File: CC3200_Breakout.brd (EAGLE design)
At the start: 58.4 x 35.2 mm, 51 parts, among them J22 M10X2, J23 M10X2, U15 AT25FS010, Y2 32.768KHz, Y3 407MHz

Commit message: proper files added now, ready to finish routing
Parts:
- added C1, C11, C13, C14, C16, C17, C19, C21, C22, C5, C51, C9: 0.1uF, SparkFun-Capacitors:0402
- added C10, C12, C2, C20, C6: 1.0uF, SparkFun-Capacitors:0402
- added C15, C18: 4.7nF, SparkFun-Retired:0603
- added C3, C4, C7: 10uF, SparkFun-Capacitors:0603
- added C46, C49: 47uF, SparkFun-Capacitors:0603
- added C52: 100uF, SparkFun-Capacitors:PANASONIC_D
- added C53: 0.1uF, resistor:C0402K
- added D1: 1A/30V, diode:SMB
- added FB1, FB2: 40Ω/1.5A, SparkFun-Coils:0603
- added J1: MJ-3536N, con-cuistack:MJ-3536N
- added J2: (no value), SparkFun-Connectors:USB-MICROB
- added J3, J4: SJ-3515-SMT, con-cuistack:SJ-3515-SMT
- added JMP1, JMP2, JMP3, JMP4, JMP5: 0R-JUMPA, jump-0r-smd:A0R-JMP
- added JP1: (no value), SparkFun-Retired:1X02
- added R2, R5, R7: 10k, SparkFun-Resistors:0603
- added R3, R4: 1k, SparkFun-Resistors:0603
- added TERMINAL_BLOCK: (no value), SparkFun-Connectors:JST-4-PTH
- added TP1, TP13, TP2, TP3: (no value), SparkFun-Connectors:1X01
- added U1: TLV320AIC3254_RHB_32, TLV320AIC3254:RHB32_3P45X3P45
- added U2: TPA2012D2_RTJ_20, TPA2012D2_RTJ_20:RTJ20_2P7X2P7
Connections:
- removed net 50: J22.20, U$1.50
- removed net 53: J22.16, U$1.53
- removed net 61: J22.9, U$1.61
- removed net 63: J22.14, U$1.63
- removed net 64: J22.18, U$1.64
- removed net N$91: J23.10
- new net +3V3: C5.1, C6.1, U1.26
- new net AA_LOL: R4.2, U1.22
- new net AA_LOR: R3.2, U1.23
- new net BCLK_IN: JMP3.2, TP13.1, U1.1, U1.2
- new net BCLK_J3: J22.16, JMP3.1, U$1.53
- new net CODEC_RESET: J22.9, JMP1.3, U$1.61
- new net DIN: JMP4.1, JMP5.3, U1.4
- new net DIN_J3: J22.18, JMP4.2, U$1.64
- new net DOUT: JMP4.3, JMP5.1, U1.5
- new net DOUT_J3: J22.20, JMP5.2, U$1.50
- new net FSYNC_IN: JMP2.2, U1.3
- new net FSYNC_J3: J22.14, JMP2.1, U$1.63
- new net LOUT1: TERMINAL_BLOCK.4, U2.2
- new net LOUT2: TERMINAL_BLOCK.3, U2.5
- new net MASTER_RESET: C53.1, J23.10, JMP1.1, R7.1
- new net MICBIAS: R5.2, U1.19
- new net N$23: TP2.1, U1.11
- new net N$25: C3.1, U1.18
- new net N$26: TP1.1, U1.8
- new net N$34: TP3.1, U1.32
- new net N$35: JP1.2, R2.2, U2.1
- new net N$37: C7.1, U1.29
- new net N$38: C22.2, J4.3, J4.4
- new net N$39: C14.2, U2.20
- new net N$41: C13.1, C15.1, R3.1
- new net N$42: C13.2, U2.19
- new net N$43: C16.2, U2.17
- new net N$44: C16.1, C18.1, R4.1
- new net N$45: C17.2, U2.16
- new net N$46: C21.2, J4.1, J4.2
- new net N$55: C46.2, J3.1, J3.2
- new net N$56: C49.2, J3.3, J3.4
- new net N$57: C51.2, J1.2, J1.3, R5.1
- new net N$58: D1.A, FB2.2
- new net N$59: FB2.1, J2.VBUS
- new net N$60: FB1.2, J2.GND
- new net RESET_OUT: JMP1.2, U1.31
- new net ROUT1: TERMINAL_BLOCK.2, U2.14
- new net ROUT2: TERMINAL_BLOCK.1, U2.11
- new net SJ_HPL: C49.1, U1.25
- new net SJ_HPR: C46.1, U1.27
- new net SJ_IN1L: C21.1, U1.13
- new net SJ_IN1R: C22.1, U1.14
- new net SJ_IN2L: U1.15
- new net SJ_IN2R: C51.1, U1.16
- new net SJ_IN3L: U1.20
- new net SJ_IN3R: U1.21
- new net VCCA: C4.1, U1.24, U2.7, U2.8
- new net VCC_5V_MCU: D1.C
- new net VCC_BRD1: C1.1, C10.1, C11.1, C12.1, C19.1, C2.1, C20.1, C52.+, C9.1, JP1.1, U1.30, U1.6, U2.13, U2.3, U2.9
- net 3.3V: now also R7.2
- net GND: now also C1.2, C10.2, C11.2, C12.2, C14.1, C15.2, C17.1, C18.2, C19.2, C2.2, C20.2, C3.2, C4.2, C5.2, C52.-, C53.2, C6.2, C7.2, C9.2, FB1.1, J1.1, J2.MT1, J2.MT2, J2.P$1, J2.P$2, J3.5, J4.5, R2.1, U1.12, U1.17, U1.28, U1.33, U1.7, U2.12, U2.15, U2.18, U2.21, U2.4
- net SCL: now also U1.9
- net SDA: now also U1.10
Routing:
- net DOUT_J3: track 0.00 -> 60.7 mm, vias 0 -> 1
- net 50: track 60.7 -> 0.00 mm, vias 1 -> 0
- net BCLK_J3: track 0.00 -> 45.4 mm, vias 0 -> 3
- net 53: track 45.4 -> 0.00 mm, vias 3 -> 0
- net DIN_J3: track 0.00 -> 27.4 mm, vias 0 -> 1
- net 64: track 27.4 -> 0.00 mm, vias 1 -> 0
- net FSYNC_J3: track 0.00 -> 24.1 mm, vias 0 -> 1
- net 63: track 24.1 -> 0.00 mm, vias 1 -> 0
- net CODEC_RESET: track 0.00 -> 24.1 mm, vias 0 -> 1
- net 61: track 24.1 -> 0.00 mm, vias 1 -> 0
- removed copper zone on layer 1, net GND
- removed copper zone on layer 2, net GND
- removed copper zone on layer 16, net VCC_BRD
- removed copper zone on layer 15, net V_BATT
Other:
- board size 58.4 x 35.2 mm -> 76.2 x 50.8 mm

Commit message: routed
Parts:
- moved JMP1 399.8 mm to (13.5, 69.6), turned to 270 degrees
- moved R7 387.3 mm to (35.0, 37.2), turned to 270 degrees
- moved C53 383.2 mm to (31.6, 37.6), turned to 270 degrees
- moved JMP4 367.9 mm to (19.2, 50.8)
- moved JMP5 366.8 mm to (18.9, 40.7)
- moved JMP2 362.1 mm to (21.3, 61.3)
- moved JMP3 349.7 mm to (14.2, 42.0), turned to 180 degrees
- moved D1 324.9 mm to (59.1, 22.5), turned to 270 degrees
- moved FB2 316.8 mm to (61.5, 14.2), turned to 90 degrees
- moved J2 314.1 mm to (59.7, 3.81), turned to 90 degrees
- moved FB1 312.0 mm to (58.5, 13.7), turned to 270 degrees
- moved C49 288.9 mm to (10.6, 73.6), turned to 180 degrees
- moved C46 287.5 mm to (18.0, 73.5), turned to 90 degrees
- moved C21 285.1 mm to (31.2, 73.5), turned to 90 degrees
- moved C52 272.4 mm to (4.39, 69.4), turned to 180 degrees
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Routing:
- net GND: track 9.93 -> 766.8 mm, vias 49 -> 67
- net VCC_BRD1: track 0.00 -> 121.2 mm, vias 0 -> 5
- net MASTER_RESET: track 0.00 -> 86.5 mm, vias 0 -> 2
- net SCL: track 30.5 -> 107.8 mm, vias 1 -> 2
- net N$35: track 0.00 -> 74.0 mm, vias 0 -> 2
- net FSYNC_J3: track 24.1 -> 88.3 mm, vias 1 -> 3
- net SDA: track 32.2 -> 95.2 mm, vias 1 -> 2
- net DIN_J3: track 27.4 -> 90.2 mm, vias 1 -> 3
- net V_BATT: track 94.1 -> 153.0 mm, vias 8 -> 13
- net N$45: track 0.00 -> 55.2 mm, vias 0 -> 2
- net CODEC_RESET: track 24.1 -> 75.2 mm, vias 1 -> 4
- net BCLK_IN: track 0.00 -> 45.6 mm, vias 0 -> 1
- net SJ_IN1L: track 0.00 -> 39.0 mm, vias 0 -> 2
- net SJ_HPL: track 0.00 -> 32.2 mm, vias 0 -> 2
- net SJ_IN1R: track 0.00 -> 30.5 mm
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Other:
- board size 76.2 x 50.8 mm -> 76.2 x 88.9 mm

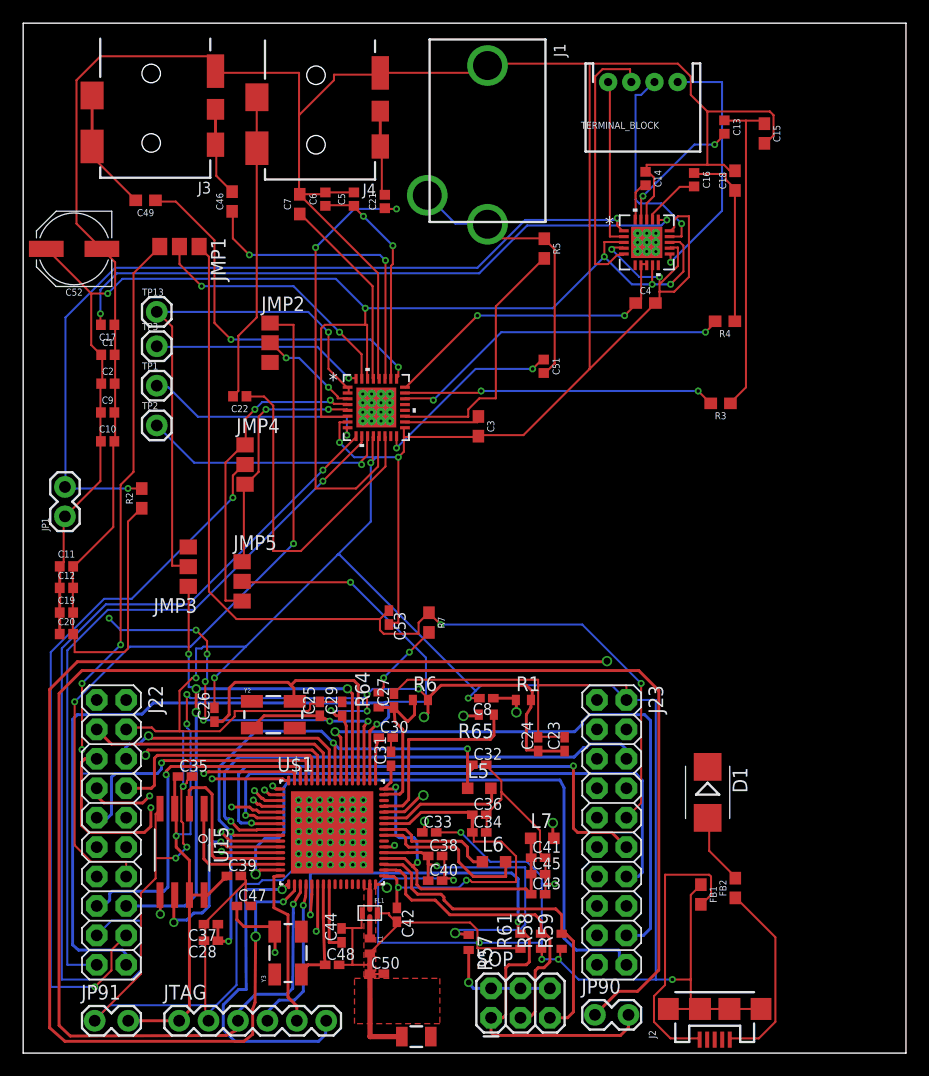
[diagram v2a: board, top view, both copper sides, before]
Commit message: routing finished, BOM added
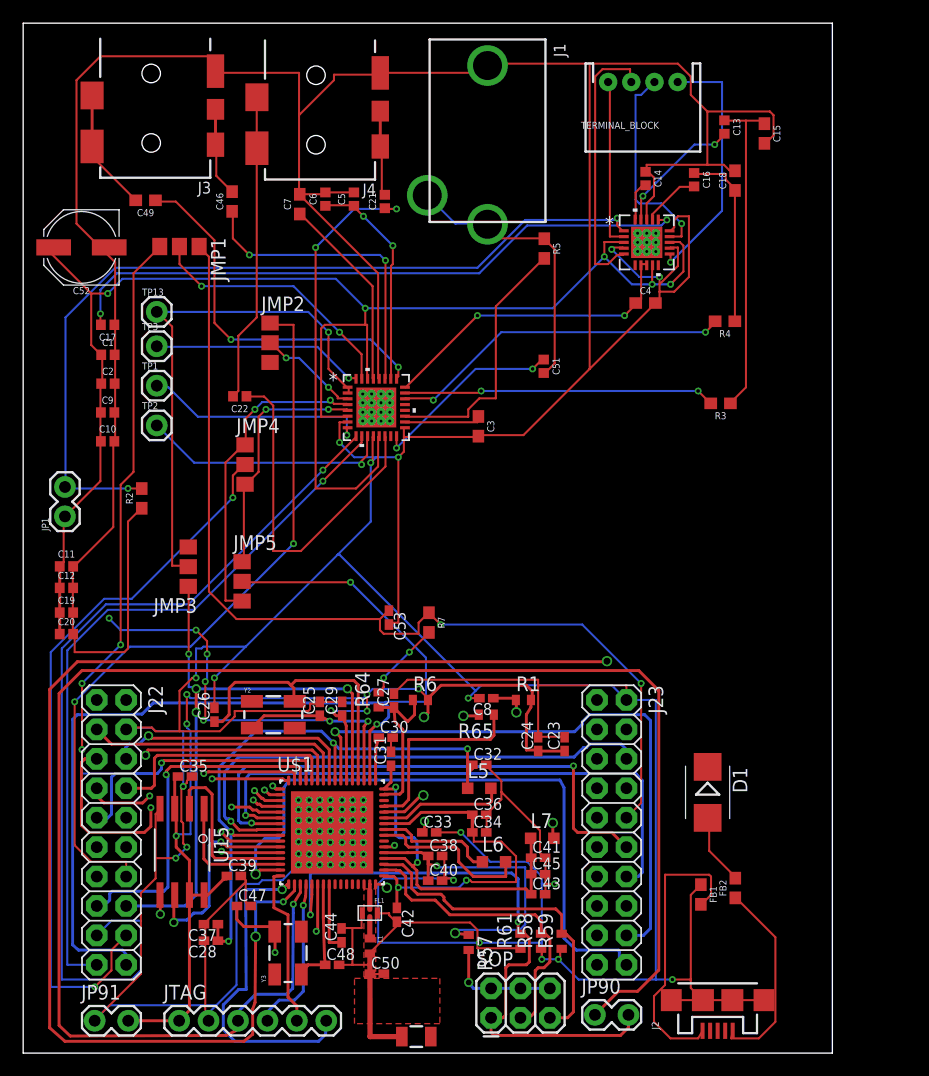
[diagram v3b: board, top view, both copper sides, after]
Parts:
- moved J2 0.80 mm to (59.9, 4.57)
- moved C52 0.65 mm to (5.03, 69.5)
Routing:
- net N$60: track 24.5 -> 25.1 mm
- net VCC_BRD1: track 121.2 -> 121.7 mm
- net GND: track 766.8 -> 767.3 mm
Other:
- board size 76.2 x 88.9 mm -> 69.8 x 88.9 mm
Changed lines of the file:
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@@
 <board>
 <plain>
-<wire x1="0" y1="0" x2="76.2" y2="0" width="0" layer="20"/>
-<wire x1="76.2" y1="0" x2="76.2" y2="88.9" width="0" layer="20"/>
-<wire x1="76.2" y1="88.9" x2="0" y2="88.9" width="0" layer="20"/>
+<wire x1="0" y1="0" x2="69.85" y2="0" width="0" layer="20"/>
+<wire x1="69.85" y1="0" x2="69.85" y2="88.9" width="0" layer="20"/>
+<wire x1="69.85" y1="88.9" x2="0" y2="88.9" width="0" layer="20"/>
 <wire x1="0" y1="88.9" x2="0" y2="0" width="0" layer="20"/>
 </plain>
@@
 <attribute name="PROD_ID" value="RES-00824" x="44.9834" y="69.4436" size="1.778" layer="27" rot="R270" display="off"/>
 </element>
-<element name="C52" library="SparkFun-Capacitors" package="PANASONIC_D" value="100uF" x="4.3942" y="69.4182" rot="R180">
-<attribute name="PROD_ID" value="CAP-12547" x="4.3942" y="69.4182" size="1.778" layer="27" rot="R180" display="off"/>
+<element name="C52" library="SparkFun-Capacitors" package="PANASONIC_D" value="100uF" x="5.0292" y="69.5452" rot="R180">
+<attribute name="PROD_ID" value="CAP-12547" x="5.0292" y="69.5452" size="1.778" layer="27" rot="R180" display="off"/>
 </element>
 <element name="TERMINAL_BLOCK" library="SparkFun-Connectors" package="JST-4-PTH" value="" x="53.4924" y="83.82" rot="R180">
@@
 </element>
 <element name="D1" library="diode" package="SMB" value="1A/30V" x="59.0804" y="22.5044" rot="R270"/>
-<element name="J2" library="SparkFun-Connectors" package="USB-MICROB" value="" x="59.69" y="3.81" rot="R90">
-<attribute name="PROD_ID" value="CONN-09505" x="59.69" y="3.81" size="1.778" layer="27" rot="R90" display="off"/>
-<attribute name="SF_ID" value="PRT-08533" x="59.69" y="3.81" size="1.778" layer="27" rot="R90" display="off"/>
+<element name="J2" library="SparkFun-Connectors" package="USB-MICROB" value="" x="59.944" y="4.572" rot="R90">
+<attribute name="PROD_ID" value="CONN-09505" x="59.944" y="4.572" size="1.778" layer="27" rot="R90" display="off"/>
+<attribute name="SF_ID" value="PRT-08533" x="59.944" y="4.572" size="1.778" layer="27" rot="R90" display="off"/>
 </element>
 <element name="JMP2" library="jump-0r-smd" package="A0R-JMP" value="0R-JUMPA" x="21.3106" y="61.3156"/>
@@
 <wire x1="7.9375" y1="68.2625" x2="6.82625" y2="69.37375" width="0.1778" layer="1"/>
 <wire x1="7.9375" y1="62.865" x2="7.9375" y2="68.2625" width="0.1778" layer="1"/>
-<wire x1="6.82625" y1="69.37375" x2="6.7942" y2="69.4182" width="0.1778" layer="1"/>
+<wire x1="6.82625" y1="69.37375" x2="7.4292" y2="69.5452" width="0.1778" layer="1"/>
 <wire x1="7.9375" y1="62.865" x2="7.8698" y2="62.865" width="0.1778" layer="1"/>
 <wire x1="7.77875" y1="45.4025" x2="4.445" y2="42.06875" width="0.1778" layer="1"/>
@@
 <wire x1="16.51" y1="86.0425" x2="6.6675" y2="86.0425" width="0.1778" layer="1"/>
 <wire x1="16.51" y1="84.7725" x2="16.51" y2="86.0425" width="0.1778" layer="1"/>
-<wire x1="6.6675" y1="69.5325" x2="6.7942" y2="69.4182" width="0.1778" layer="1"/>
+<wire x1="6.6675" y1="69.5325" x2="7.4292" y2="69.5452" width="0.1778" layer="1"/>
 <wire x1="16.51" y1="84.7725" x2="16.6006" y2="84.7594" width="0.1778" layer="1"/>
 <wire x1="26.82875" y1="84.455" x2="30.7975" y2="84.455" width="0.1778" layer="1"/>
@@
 <wire x1="30.7975" y1="84.455" x2="30.8246" y2="84.607" width="0.1778" layer="1"/>
 <wire x1="57.62625" y1="13.6525" x2="58.42" y2="14.44625" width="0.1778" layer="1"/>
-<wire x1="57.62625" y1="4.60375" x2="57.62625" y2="6.35" width="0.1778" layer="1"/>
-<wire x1="57.62625" y1="6.35" x2="57.62625" y2="13.6525" width="0.1778" layer="1"/>
+<wire x1="57.62625" y1="13.6525" x2="57.62625" y2="6.35" width="0.1778" layer="1"/>
 <wire x1="58.42" y1="14.44625" x2="58.4962" y2="14.5406" width="0.1778" layer="1"/>
-<wire x1="57.62625" y1="3.81" x2="55.69" y2="3.81" width="0.1778" layer="1"/>
-<wire x1="57.62625" y1="4.60375" x2="57.62625" y2="3.81" width="0.1778" layer="1"/>
-<wire x1="57.62625" y1="4.60375" x2="58.42" y2="3.81" width="0.1778" layer="1"/>
-<wire x1="58.42" y1="3.81" x2="60.96" y2="3.81" width="0.1778" layer="1"/>
-<wire x1="60.96" y1="3.81" x2="63.69" y2="3.81" width="0.1778" layer="1"/>
+<wire x1="58.674" y1="4.572" x2="61.214" y2="4.572" width="0.1778" layer="1"/>
+<wire x1="61.214" y1="4.572" x2="63.944" y2="4.572" width="0.1778" layer="1"/>
 <wire x1="29.21" y1="10.795" x2="28.41625" y2="10.795" width="0.1778" layer="1"/>
 <wire x1="28.41625" y1="10.795" x2="27.6225" y2="10.795" width="0.1778" layer="1"/>
@@
 <wire x1="31.75" y1="27.14625" x2="31.75" y2="26" width="0.1778" layer="1"/>
 <wire x1="31.75" y1="27.14625" x2="31.8928" y2="27.2288" width="0.1778" layer="1"/>
+<wire x1="55.944" y1="4.572" x2="58.674" y2="4.572" width="0.1778" layer="1"/>
+<wire x1="57.62625" y1="6.35" x2="57.62625" y2="5.61975" width="0.1778" layer="1"/>
+<wire x1="57.62625" y1="5.61975" x2="58.674" y2="4.572" width="0.1778" layer="1"/>
 <wire x1="53.8226" y1="71.952" x2="53.8226" y2="69.977" width="0" layer="19" extent="1-1"/>
 <wire x1="30.48" y1="55.7276" x2="30.7300625" y2="58.2026" width="0" layer="19" extent="1-1"/>
@@
 <wire x1="61.11875" y1="1.27" x2="63.5" y2="1.27" width="0.1778" layer="1"/>
 <wire x1="61.595" y1="13.335" x2="61.468" y2="13.3994" width="0.1778" layer="1"/>
-<wire x1="61.11875" y1="1.27" x2="60.99" y2="1.16" width="0.1778" layer="1"/>
+<wire x1="61.11875" y1="1.27" x2="61.244" y2="1.922" width="0.1778" layer="1"/>
 </signal>
 <signal name="N$60">
@@
 <wire x1="58.26125" y1="1.27" x2="55.88" y2="1.27" width="0.1778" layer="1"/>
 <wire x1="58.57875" y1="12.85875" x2="58.4962" y2="12.8406" width="0.1778" layer="1"/>
-<wire x1="58.26125" y1="1.27" x2="58.39" y2="1.16" width="0.1778" layer="1"/>
+<wire x1="58.26125" y1="1.27" x2="58.644" y2="1.922" width="0.1778" layer="1"/>
 </signal>
 <signal name="FSYNC_J3">
@@
 <wire x1="5.87375" y1="61.11875" x2="5.87375" y2="65.56375" width="0.1778" layer="1"/>
 <wire x1="6.6675" y1="60.325" x2="5.87375" y2="61.11875" width="0.1778" layer="1"/>
-<wire x1="2.06375" y1="69.37375" x2="1.9942" y2="69.4182" width="0.1778" layer="1"/>
+<wire x1="2.06375" y1="69.37375" x2="2.6292" y2="69.5452" width="0.1778" layer="1"/>
 <wire x1="6.6675" y1="60.325" x2="6.7352" y2="60.2742" width="0.1778" layer="1"/>
 <wire x1="6.6675" y1="49.37125" x2="3.65125" y2="46.355" width="0.1778" layer="1"/>

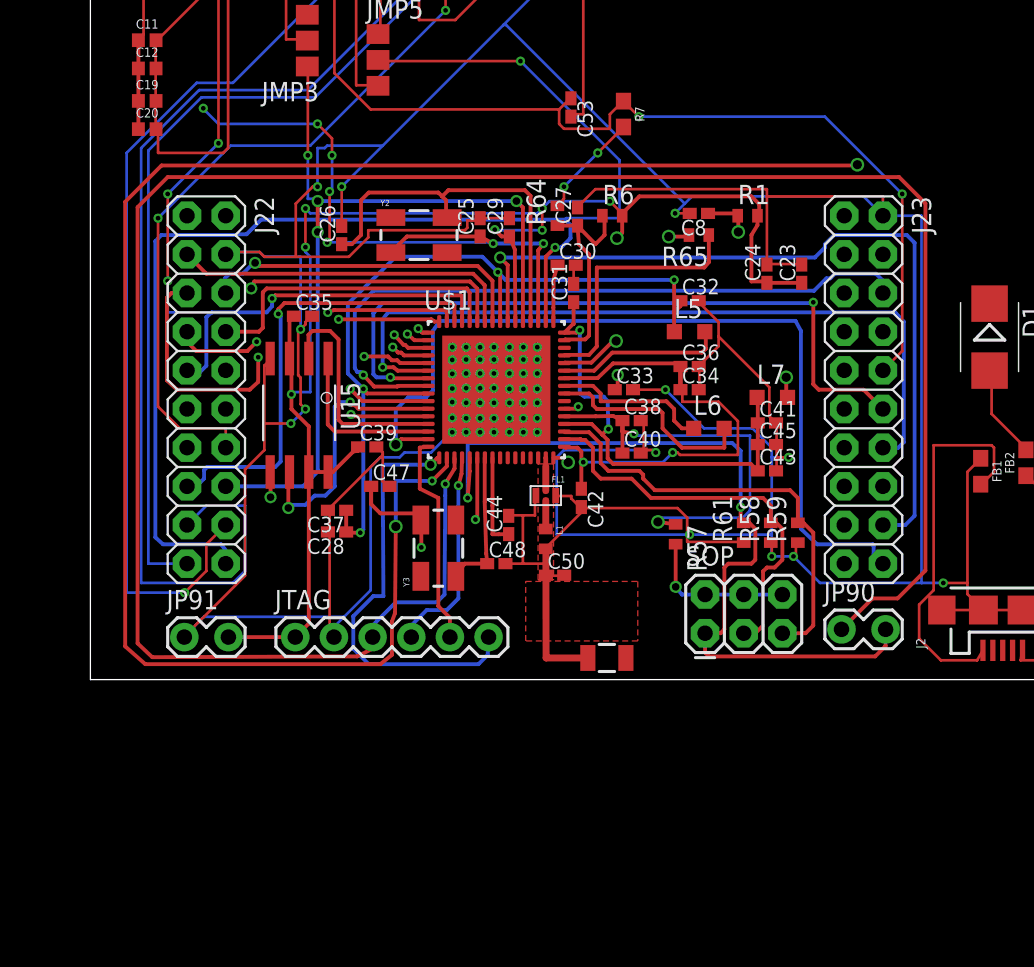
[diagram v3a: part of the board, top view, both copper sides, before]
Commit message: before ripup and change to two layers
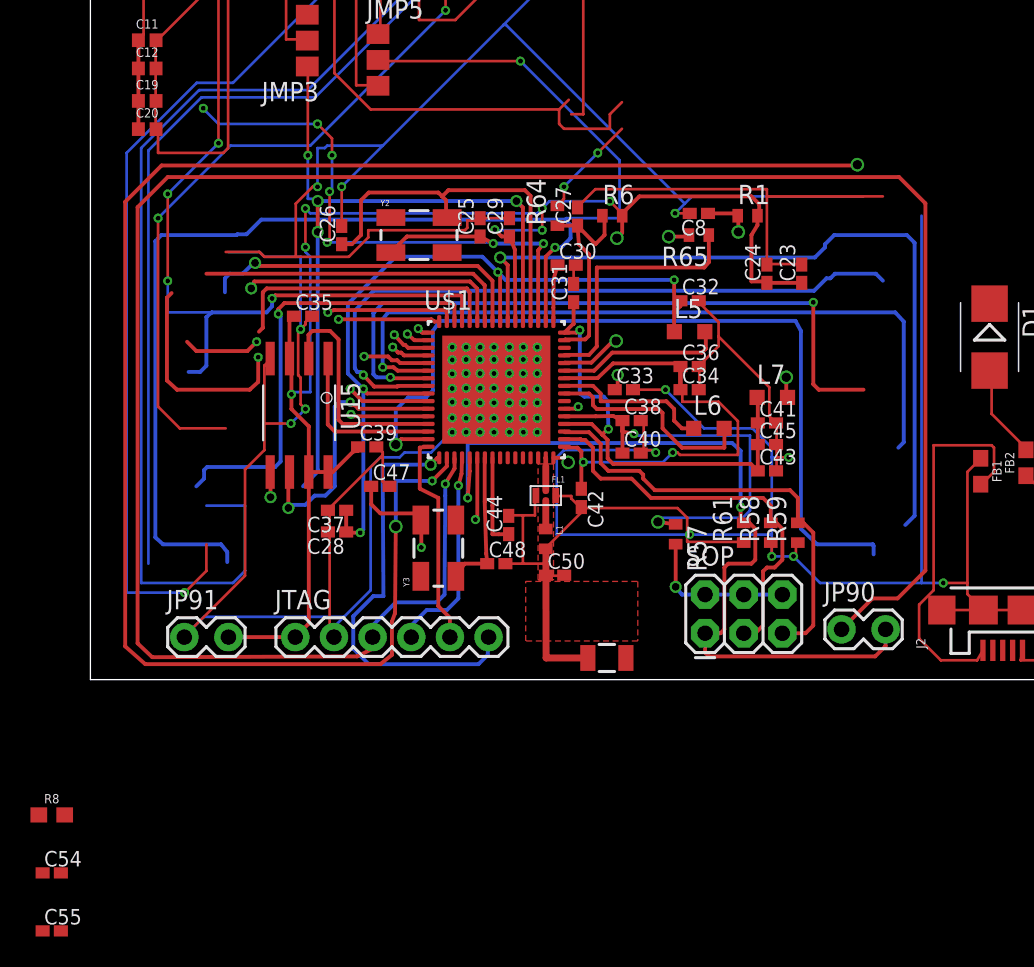
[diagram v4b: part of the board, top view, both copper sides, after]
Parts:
- removed C53: 0.1uF, resistor:C0402K
- removed J22, J23: M10X2, SparkFun-Connectors:2X10
- removed R7: 10k, SparkFun-Resistors:0603
- added C54, C55: 0.1uF, resistor:C0402K
- added R8: 10k, SparkFun-Resistors:0603
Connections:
- removed net 16: J23.17
- removed net 17: J23.19
- removed net 21: J23.16
- removed net N$47: J23.1
- removed net N$48: J23.3
- removed net N$49: J23.5
- removed net N$50: J23.7
- removed net N$51: J23.9
- removed net N$52: J23.11
- removed net N$53: J23.13
- removed net N$54: J23.15
- removed net N$81: J22.10
- removed net N$82: J22.12
- removed net VCC_BRD: J22.1
- removed net VCC_MCU_5V: J22.2
- net 15: no longer J23.20
- net 18: no longer J23.4
- net 3: no longer J22.7
- net 3.3V: no longer R7.2
- net 4: no longer J22.5
- net 45: no longer J23.8
- net 55: no longer J23.18
- net 57: no longer J22.6
- net 58: no longer J22.3
- net 59: no longer J22.11
- net 60: no longer J22.8
- net 62: no longer J22.15
- net BCLK_J3: no longer J22.16
- net CODEC_RESET: no longer J22.9
- net DIN_J3: no longer J22.18
- net DOUT_J3: no longer J22.20
- net FSYNC_J3: no longer J22.14
- net GND: now also C54.2; no longer C53.2, J22.4, J23.2
- net MASTER_RESET: now also C54.1, R8.1; no longer C53.1, J23.10, R7.1
- net SCL: no longer J22.17
- net SDA: no longer J22.19
- net SPI_CLK: no longer J22.13
- net SPI_CS: no longer J23.6
- net SPI_MISO: no longer J23.14
- net SPI_MOSI: no longer J23.12
- net VCC_BRD1: now also R8.2
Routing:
- net MASTER_RESET: track 86.5 -> 53.3 mm, vias 2 -> 0
- net GND: track 767.3 -> 761.2 mm
- net BCLK_J3: track 54.9 -> 49.8 mm
- net SDA: track 95.2 -> 91.2 mm
- net SCL: track 107.8 -> 104.5 mm
- net 60: track 20.6 -> 18.4 mm
- net DIN_J3: track 90.2 -> 88.4 mm
- net SPI_MOSI: track 47.6 -> 45.8 mm
- net 58: track 22.8 -> 21.0 mm
- net 18: track 118.9 -> 117.1 mm
- net 55: track 52.9 -> 51.4 mm
- net 45: track 22.8 -> 21.3 mm
- net FSYNC_J3: track 88.3 -> 87.0 mm
- net 4: track 26.6 -> 25.6 mm
- net SPI_MISO: track 50.4 -> 49.4 mm
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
